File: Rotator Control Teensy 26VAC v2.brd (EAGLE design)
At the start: 88.9 x 81.3 mm, 61 parts, among them K1 G5LE, K2 G5LE, K3 G5LE, Q1 BSS123, Q2 BSS123, Q3 BSS123, U1 MAX7221EWG+T, X1 Rotor, X2 26VAC

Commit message: Version 2 sent to OSHPark Add pullup on ISET Tweaked a bunch of layout, unecessarily
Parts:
- added R2: 39K, rcl:R0603
- moved C16 6.12 mm to (45.7, 61.7), turned to 90 degrees
- moved D1 1.80 mm to (33.0, 61.0), turned to 180 degrees
- moved R19 0.76 mm to (14.1, 5.08)
- moved D3 0.51 mm to (17.9, 10.2)
- moved R20 0.25 mm to (21.3, 11.4)
- turned R5 to 90 degrees
- turned R6 to 90 degrees
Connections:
- new net ISET: R2.2, U1.18
- net +5V: now also R2.1
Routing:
- net MISO: track 87.9 -> 79.0 mm
- net LEFT: track 44.3 -> 38.6 mm
- net CS: track 66.2 -> 60.6 mm
- net SCK: track 56.6 -> 51.4 mm, vias 4 -> 3
- net 3V3: track 111.6 -> 107.0 mm
- net SEGG: track 32.6 -> 28.3 mm, vias 2 -> 1
- net MOSI: track 88.1 -> 84.0 mm
- net SEGE: track 37.0 -> 33.3 mm, vias 1 -> 0
- net BRAKE: track 42.3 -> 38.6 mm
- net WIPER+: track 96.1 -> 92.7 mm
- net SEGC: track 28.9 -> 25.6 mm, vias 1 -> 0
- net +5V: track 141.5 -> 144.7 mm
- net SEGA: track 43.5 -> 40.4 mm
- net SEGD: track 29.1 -> 26.1 mm, vias 1 -> 0
- net DIG3: track 30.8 -> 27.8 mm, vias 3 -> 2
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
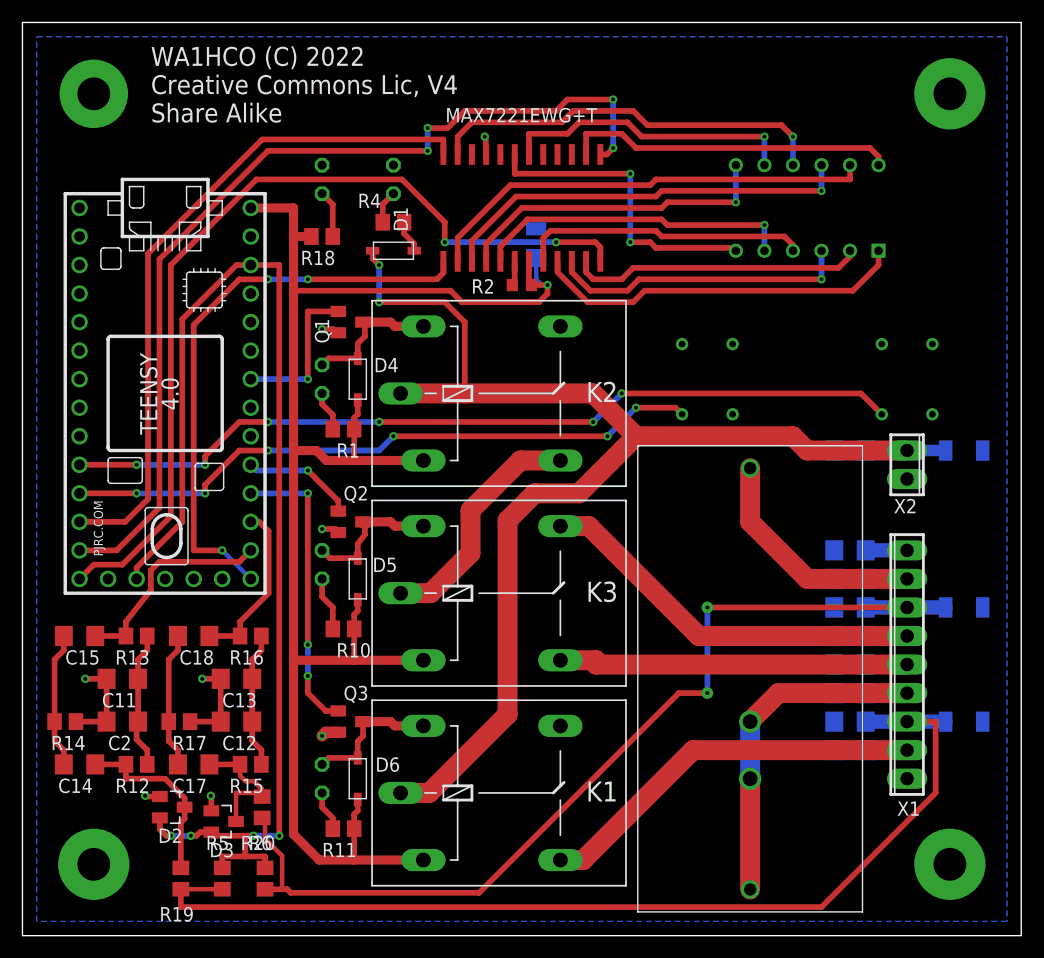
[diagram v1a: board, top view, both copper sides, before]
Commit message: Moved overvoltage protect diodes to after the 60 Hz notch filter.  So the 60 Hz doesn't cause clipping and a DC shift when DC is near zero.
Tweaked the layout accordingly.
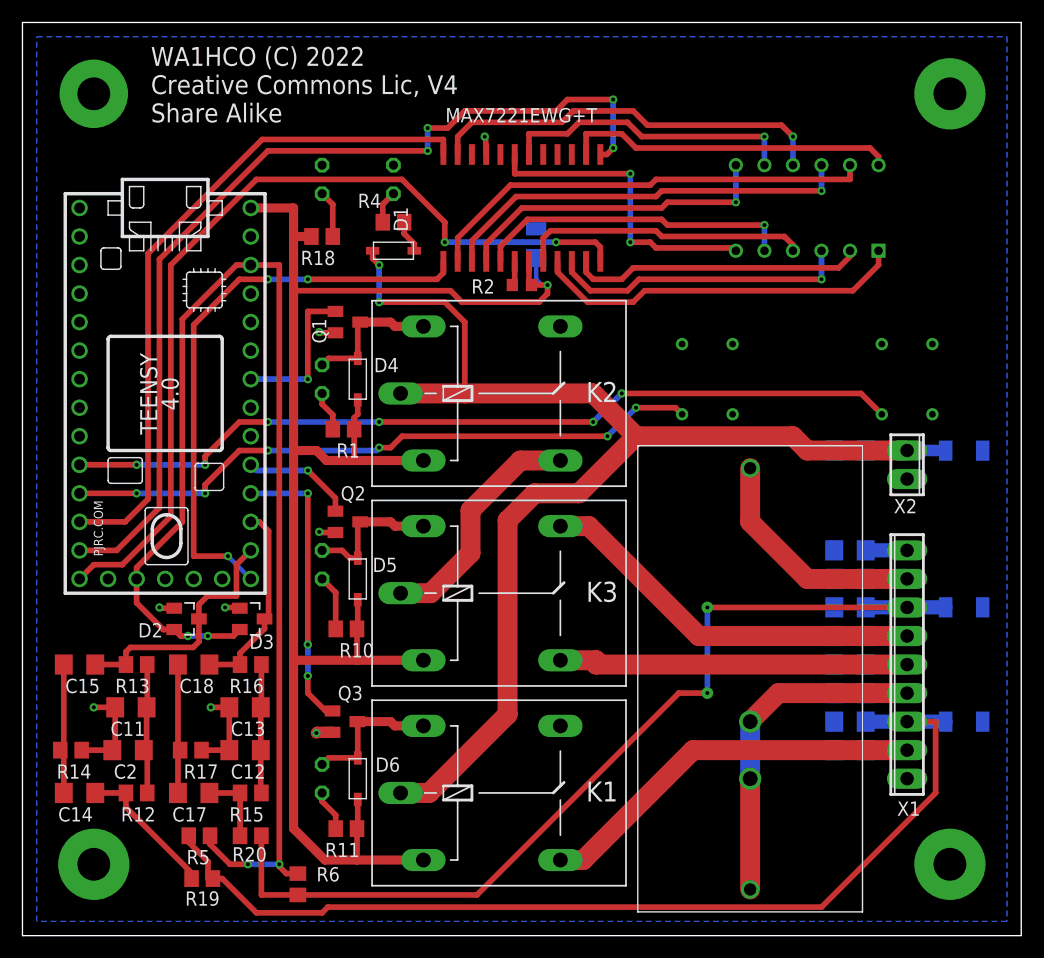
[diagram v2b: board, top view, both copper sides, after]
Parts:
- moved D3 18.2 mm to (20.4, 28.2)
- moved D2 16.8 mm to (14.6, 28.2)
- moved R5 4.32 mm to (15.7, 8.89), turned to 0 degrees
- moved R6 2.96 mm to (24.5, 4.57)
- moved R17 2.74 mm to (15.0, 16.5)
- moved R20 2.74 mm to (20.3, 8.89), turned to 180 degrees
- moved C12 2.65 mm to (19.8, 16.5)
- moved C13 2.65 mm to (19.8, 20.3)
- moved C11 2.65 mm to (9.65, 20.3)
- moved R14 2.59 mm to (4.32, 16.5)
- moved C2 2.59 mm to (9.40, 16.5)
- moved C15 2.54 mm to (5.08, 24.1)
- moved C18 2.54 mm to (15.2, 24.1)
- moved R13 2.54 mm to (10.2, 24.1)
- moved R16 2.54 mm to (20.3, 24.1)
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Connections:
- net N$1: no longer D3.3
- net N$23: now also D3.3
- net N$3: no longer D2.3
- net N$7: now also D2.3
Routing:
- net N$1: track 12.0 -> 6.54 mm
- net 3V3: track 107.0 -> 111.3 mm
- net N$3: track 16.3 -> 12.8 mm
- net N$7: track 19.0 -> 22.3 mm
- net N$23: track 15.0 -> 17.8 mm
- net WIPER+: track 92.7 -> 91.0 mm
- net WIPER-: track 86.5 -> 84.9 mm
- net N$21: track 12.1 -> 11.5 mm
- net N$22: track 12.1 -> 11.6 mm
- net N$12: track 26.2 -> 25.7 mm

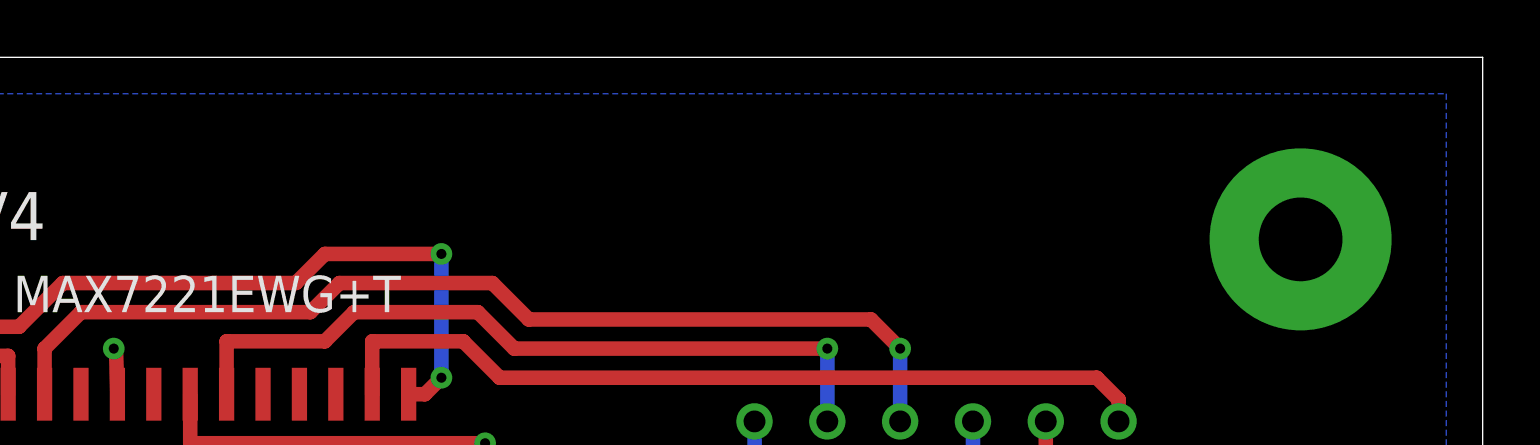
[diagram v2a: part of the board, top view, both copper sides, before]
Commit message: Move OVP diodes close to ADC
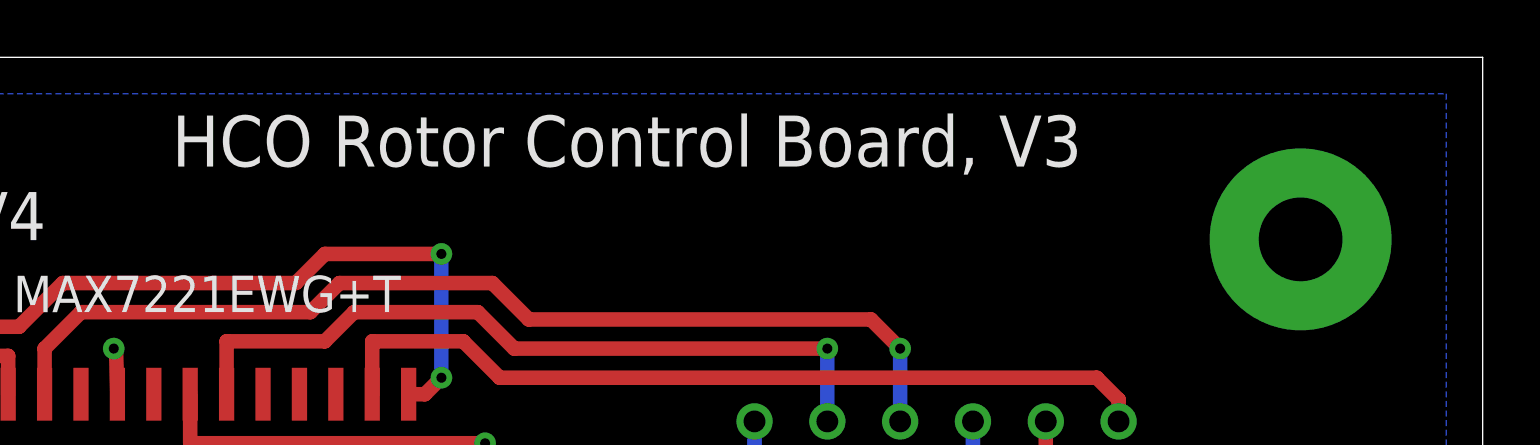
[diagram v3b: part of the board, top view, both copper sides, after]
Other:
- board text added: "HCO Rotor Control Board, V3"
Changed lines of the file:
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@@
 <text x="80.518" y="53.848" size="1.778" layer="122" rot="MR0">CW</text>
 <text x="63.754" y="53.848" size="1.778" layer="122" rot="MR0">CCW</text>
+<text x="43.18" y="77.47" size="1.778" layer="121">HCO Rotor Control Board, V3</text>
 </plain>
 <attributes>
